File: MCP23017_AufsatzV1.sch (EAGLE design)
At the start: 16 parts, among them IC1 MCP23017SP

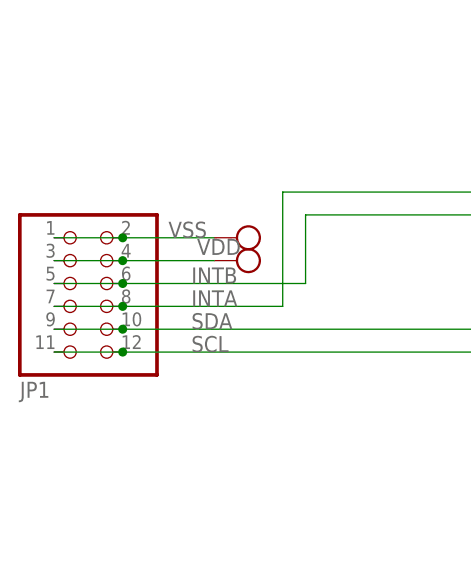
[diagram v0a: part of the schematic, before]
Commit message: Neuen 16 Fach Output und 8In8Out hinzugefügt
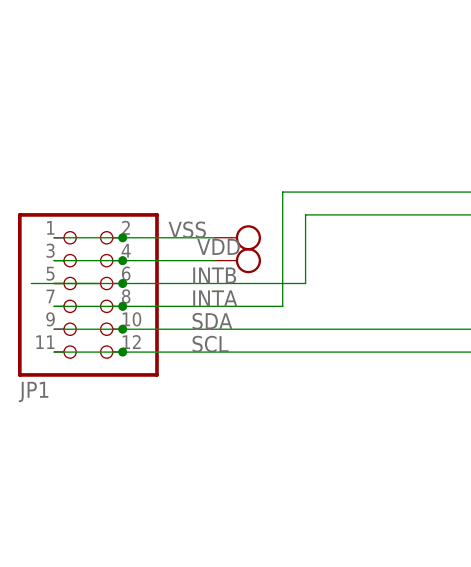
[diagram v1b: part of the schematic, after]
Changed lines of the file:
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@@
 <label x="-76.2" y="50.8" size="1.778" layer="95"/>
+</segment>
+<segment>
+<wire x1="-93.98" y1="53.34" x2="-86.36" y2="53.34" width="0.1524" layer="91"/>
 </segment>
 </net>
